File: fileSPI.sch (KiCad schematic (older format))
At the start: 6 parts, among them U18 74HC165, U25 74AHCT595, U6 74AHC273

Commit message: Renaming files, cleaning, CHANGELOG
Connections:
- net BCSPI_CLK renamed BCFG_SPI_CLK
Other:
- moved on the sheet: C41
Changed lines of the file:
@@
 L Device:C C?
 U 1 1 5DD64D25
-P 2100 3500
+P 1950 3500
 AR Path="/5ACA3361/5DD64D25" Ref="C?"  Part="1"
 AR Path="/5DD53CC6/5DD64D25" Ref="C41"  Part="1"
-F 0 "C41" H 2125 3600 50  0000 L CNN
-F 1 "10nF" H 2125 3400 50  0000 L CNN
-F 2 "Capacitor_SMD:C_0805_2012Metric" H 2138 3350 50  0001 C CNN
-F 3 "" H 2100 3500 50  0001 C CNN
-	1    2100 3500
+F 0 "C41" H 1975 3600 50  0000 L CNN
+F 1 "10nF" H 1975 3400 50  0000 L CNN
+F 2 "Capacitor_SMD:C_0805_2012Metric" H 1988 3350 50  0001 C CNN
+F 3 "" H 1950 3500 50  0001 C CNN
+	1    1950 3500
 	-1   0    0    1
 $EndComp
@@
 Wire Wire Line
 	3150 3650 3150 3600
-Wire Wire Line
-	2100 3650 3150 3650
-Wire Wire Line
-	2100 3350 2100 3300
-Wire Wire Line
-	2100 1950 3150 1950
-Wire Wire Line
-	2650 3300 2100 3300
-Connection ~ 2100 3300
 Text Label 3650 2300 0    60   ~ 0
 SPI_CFG_~PL
@@
 SPI_CLK
 Text Label 1500 1650 0    60   ~ 0
-BCSPI_CLK
+BCFG_SPI_CLK
 Text HLabel 1450 1550 0    60   Input ~ 0
 SPI_CLK
 Text HLabel 1450 1650 0    60   Input ~ 0
-BCSPI_CLK
+BCFG_SPI_CLK
 Wire Wire Line
 	1450 1550 1500 1550
@@
 Text Label 5100 3300 2    60   ~ 0
 SPI_CFG_~PL
-Text Label 2650 3200 2    60   ~ 0
-BCSPI_CLK
-Wire Wire Line
-	2100 1950 2100 3300
 Text Label 2650 2700 2    60   ~ 0
 NUMBER_4
@@
 Text Label 5100 2700 2    60   ~ 0
 BUFF_3
+Text Label 2650 3200 2    60   ~ 0
+BCFG_SPI_CLK
+Wire Wire Line
+	1950 3650 3150 3650
+Wire Wire Line
+	1950 3350 1950 3300
+Wire Wire Line
+	1950 1950 3150 1950
+Connection ~ 1950 3300
+Wire Wire Line
+	1950 3300 1950 1950
+Wire Wire Line
+	1950 3300 2650 3300
 Wire Bus Line
 	1550 4750 1550 5550

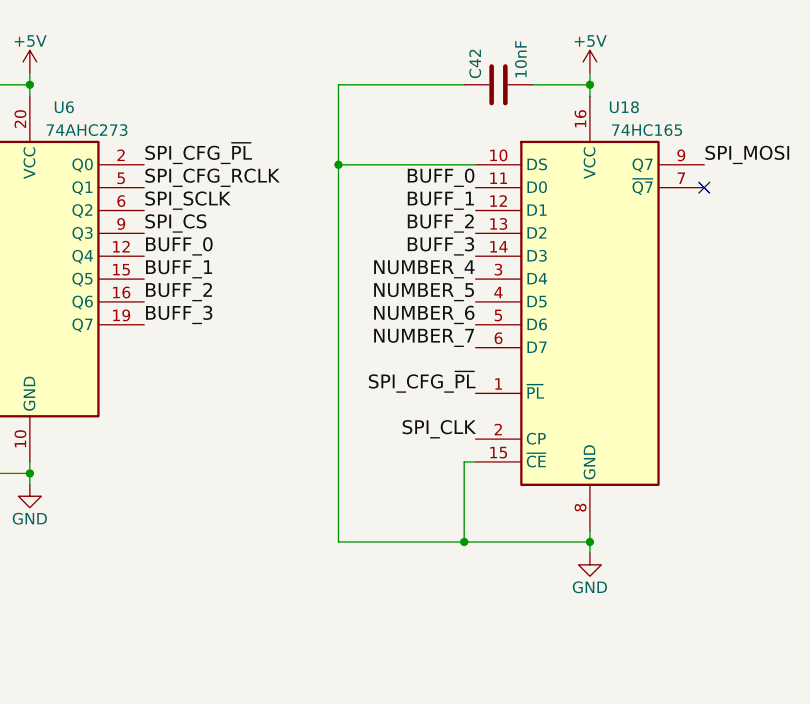
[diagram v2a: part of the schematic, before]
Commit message: Revert SPI 4bits problem work-around (finally this fixed nothing)
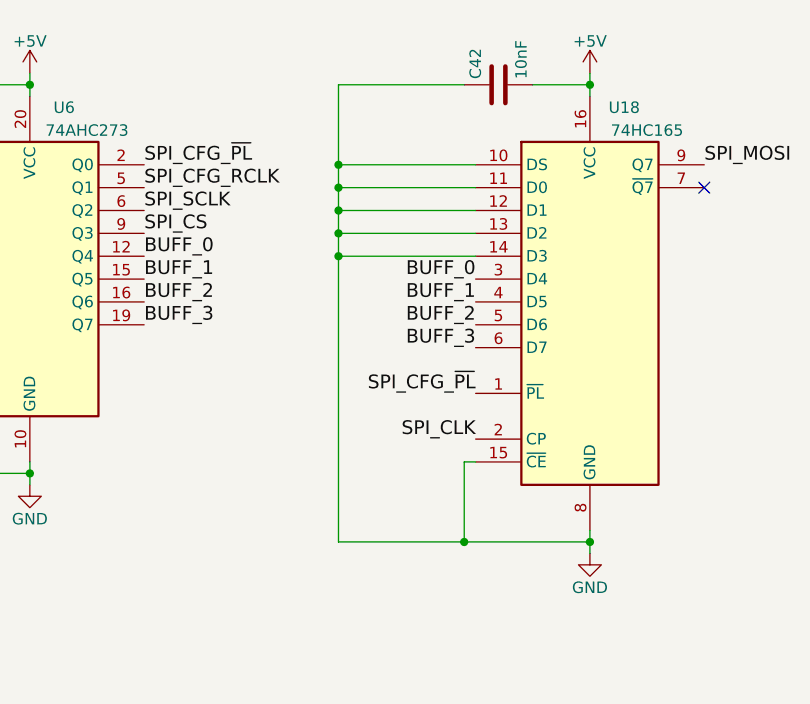
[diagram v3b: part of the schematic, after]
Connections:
- net BUFF_0: now also U18.3 (D4); no longer U18.11 (D0)
- net BUFF_1: now also U18.4 (D5); no longer U18.12 (D1)
- net BUFF_2: now also U18.5 (D6); no longer U18.13 (D2)
- net BUFF_3: now also U18.6 (D7); no longer U18.14 (D3)
- net GND: now also U18.11 (D0), U18.12 (D1), U18.13 (D2), U18.14 (D3)
- net NUMBER_4: no longer U18.3 (D4)
- net NUMBER_5: no longer U18.4 (D5)
- net NUMBER_6: no longer U18.5 (D6)
- net NUMBER_7: no longer U18.6 (D7)
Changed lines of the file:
@@
 Text Label 3650 2300 0    60   ~ 0
 SPI_CFG_~PL
-Text Label 3650 2500 0    60   ~ 0
-SPI_SCLK
 Text Label 5100 3500 2    60   ~ 0
 SPI_CLK
 Text Label 3650 2600 0    60   ~ 0
 SPI_CS
-Text Label 5100 2800 2    60   ~ 0
-NUMBER_4
-Text Label 5100 2900 2    60   ~ 0
-NUMBER_5
-Text Label 5100 3000 2    60   ~ 0
-NUMBER_6
-Text Label 5100 3100 2    60   ~ 0
-NUMBER_7
-Text Label 3650 2400 0    60   ~ 0
-SPI_CFG_RCLK
 Text Label 7500 2800 2    60   ~ 0
 SPI_CFG_RCLK
@@
 	5100 2300 4500 2300
 Wire Wire Line
-	4500 2300 4500 3950
+	4500 2300 4500 2400
 Wire Wire Line
 	4500 3950 5050 3950
@@
 Text Label 3650 3000 0    60   ~ 0
 BUFF_3
-Text Label 5100 2400 2    60   ~ 0
-BUFF_0
-Text Label 5100 2500 2    60   ~ 0
-BUFF_1
-Text Label 5100 2600 2    60   ~ 0
-BUFF_2
-Text Label 5100 2700 2    60   ~ 0
-BUFF_3
 Text Label 2650 3200 2    60   ~ 0
 BCFG_SPI_CLK
@@
 Wire Wire Line
 	1950 3300 2650 3300
+Text Label 3650 2400 0    60   ~ 0
+SPI_CFG_RCLK
+Text Label 3650 2500 0    60   ~ 0
+SPI_SCLK
+Text Label 5100 2800 2    60   ~ 0
+BUFF_0
+Text Label 5100 2900 2    60   ~ 0
+BUFF_1
+Text Label 5100 3000 2    60   ~ 0
+BUFF_2
+Text Label 5100 3100 2    60   ~ 0
+BUFF_3
+Wire Wire Line
+	5100 2400 4500 2400
+Connection ~ 4500 2400
+Wire Wire Line
+	4500 2400 4500 2500
+Wire Wire Line
+	5100 2500 4500 2500
+Connection ~ 4500 2500
+Wire Wire Line
+	4500 2500 4500 2600
+Wire Wire Line
+	5100 2600 4500 2600
+Connection ~ 4500 2600
+Wire Wire Line
+	4500 2600 4500 2700
+Wire Wire Line
+	5100 2700 4500 2700
 Wire Bus Line
 	1550 4750 1550 5550
+Connection ~ 4500 2700
+Wire Wire Line
+	4500 2700 4500 3950
 $EndSCHEMATC

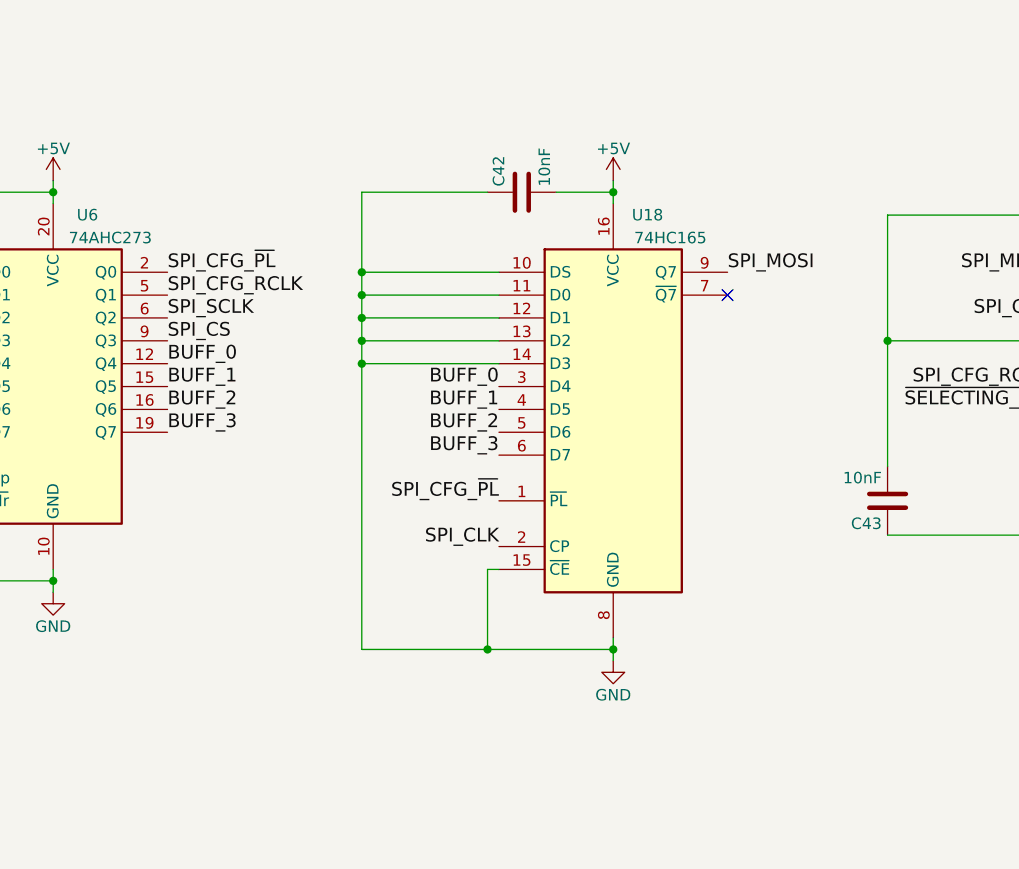
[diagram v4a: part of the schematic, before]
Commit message: V5.1 (#9)
* Apply new symbol for XC2C256-VQ100 #5

* Set new date and 5.1

* Replacing 74HC165 with 74HC166, and add SPI_CFG_DS #4

* Replace some gates with a 74AHC1G02 to fix the pulse problem #3

* Go next only if SRCVALUE, (simple instruction)

* Remove weird ghost bus in register

* Small cleaning in fileRegister

* Go next only if SRCVALUE, (complex instruction) #8
adding 74AHC1G08

* Better decoupling #6

* Component association (#7)

* netlist

* Updated BOM for V5.1

* Routing, cleaning first pass

* bit of pcb cleaning

* SolderMaskClearance to 0

* Schematics to pdf

* PCB files in pdf

* exporting Gerbert files

* new 3d images

* Update README.md

* Modifying CHANGELOG file

* Update README.md
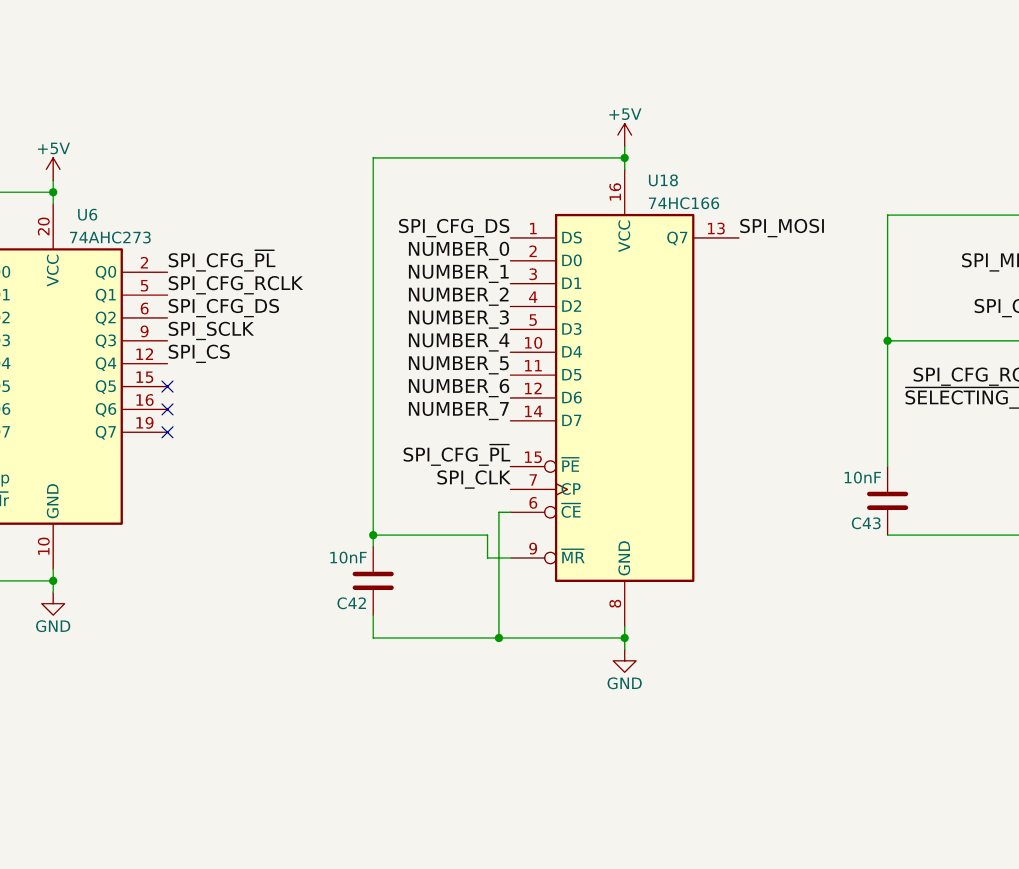
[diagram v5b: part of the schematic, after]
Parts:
- removed U18: 74HC165, Package_SO:SOIC-16_3.9x9.9mm_P1.27mm, symbol 74xx:74LS165
- added U18: 74HC166, Package_SO:SOIC-16_3.9x9.9mm_P1.27mm, symbol Custom:74HC166
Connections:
- net BUFF_0 is gone; now on net SPI_CS: U6.12 (Q4)
- net +5V: now also U18.16 (VCC), U18.9 (~MR)
- net GND: now also U18.6 (~CE), U18.8 (GND)
- net NUMBER_0: now also U18.2 (D0)
- net NUMBER_1: now also U18.3 (D1)
- net NUMBER_2: now also U18.4 (D2)
- net NUMBER_3: now also U18.5 (D3)
- net NUMBER_4: now also U18.10 (D4)
- net NUMBER_5: now also U18.11 (D5)
- net NUMBER_6: now also U18.12 (D6)
- net NUMBER_7: now also U18.14 (D7)
- net SPI_CFG_~PL: now also U18.15 (~PE)
- net SPI_CLK: now also U18.7 (CP)
- net SPI_CS: no longer U6.9 (Q3)
- net SPI_MOSI: now also U18.13 (Q7)
- net SPI_SCLK: now also U6.9 (Q3); no longer U6.6 (Q2)
- net BUFF_1: no longer names the net of U6.15 (Q5)
- net BUFF_2: no longer names the net of U6.16 (Q6)
- net BUFF_3: no longer names the net of U6.19 (Q7)
- new net SPI_CFG_DS: U18.1 (DS), U6.6 (Q2)
- no-connect marks 2 -> 4
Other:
- moved on the sheet: C42
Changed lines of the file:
@@
 Sheet 7 8
 Title "GP8B"
-Date "2020-08-19"
-Rev "V5.0"
+Date "2021-03-04"
+Rev "V5.1"
 Comp "Guillaume Guillet"
-Comment1 "Copyright Guillaume Guillet 2020"
+Comment1 "Copyright Guillaume Guillet 2021"
 Comment2 "Licensed under CERN-OHL-W v2 or later"
 Comment3 ""
 Comment4 ""
 $EndDescr
-Text Label 6100 2300 0    60   ~ 0
-SPI_MOSI
 Text Label 7500 2300 2    60   ~ 0
 SPI_MISO
@@
 F 3 "http://www.ti.com/lit/ds/symlink/sn74hc595.pdf" H 7900 2700 50  0001 C CNN
 	1    7900 2700
-	1    0    0    -1
-$EndComp
-$Comp
-L 74xx:74LS165 U18
-U 1 1 5DD58078
-P 5600 2900
-F 0 "U18" H 5750 3750 50  0000 C CNN
-F 1 "74HC165" H 5850 3650 50  0000 C CNN
-F 2 "Package_SO:SOIC-16_3.9x9.9mm_P1.27mm" H 5600 2900 50  0001 C CNN
-F 3 "http://www.ti.com/lit/gpn/sn74LS165" H 5600 2900 50  0001 C CNN
-	1    5600 2900
 	1    0    0    -1
 $EndComp
@@
 Text Label 3650 2300 0    60   ~ 0
 SPI_CFG_~PL
-Text Label 5100 3500 2    60   ~ 0
-SPI_CLK
-Text Label 3650 2600 0    60   ~ 0
+Text Label 3650 2700 0    60   ~ 0
 SPI_CS
 Text Label 7500 2800 2    60   ~ 0
@@
 L power:+5V #PWR?
 U 1 1 5DD8BC4C
-P 5600 1900
+P 5650 1750
 AR Path="/5ACA3361/5DD8BC4C" Ref="#PWR?"  Part="1"
 AR Path="/5DD53CC6/5DD8BC4C" Ref="#PWR0135"  Part="1"
-F 0 "#PWR0135" H 5600 1750 50  0001 C CNN
-F 1 "+5V" H 5600 2040 50  0000 C CNN
-F 2 "" H 5600 1900 50  0001 C CNN
-F 3 "" H 5600 1900 50  0001 C CNN
-	1    5600 1900
+F 0 "#PWR0135" H 5650 1600 50  0001 C CNN
+F 1 "+5V" H 5650 1890 50  0000 C CNN
+F 2 "" H 5650 1750 50  0001 C CNN
+F 3 "" H 5650 1750 50  0001 C CNN
+	1    5650 1750
 	1    0    0    -1
 $EndComp
@@
 L power:GND #PWR?
 U 1 1 5DD8C055
-P 5600 4000
+P 5650 3950
 AR Path="/5ACA3361/5DD8C055" Ref="#PWR?"  Part="1"
 AR Path="/5DD53CC6/5DD8C055" Ref="#PWR0136"  Part="1"
-F 0 "#PWR0136" H 5600 3750 50  0001 C CNN
-F 1 "GND" H 5600 3850 50  0000 C CNN
-F 2 "" H 5600 4000 50  0001 C CNN
-F 3 "" H 5600 4000 50  0001 C CNN
-	1    5600 4000
+F 0 "#PWR0136" H 5650 3700 50  0001 C CNN
+F 1 "GND" H 5650 3800 50  0000 C CNN
+F 2 "" H 5650 3950 50  0001 C CNN
+F 3 "" H 5650 3950 50  0001 C CNN
+	1    5650 3950
 	1    0    0    -1
 $EndComp
@@
 L Device:C C?
 U 1 1 5DD8C9C7
-P 5200 1950
+P 4550 3650
 AR Path="/5ACA3361/5DD8C9C7" Ref="C?"  Part="1"
 AR Path="/5DD53CC6/5DD8C9C7" Ref="C42"  Part="1"
-F 0 "C42" H 5225 2050 50  0000 L CNN
-F 1 "10nF" H 5225 1850 50  0000 L CNN
-F 2 "Capacitor_SMD:C_0805_2012Metric" H 5238 1800 50  0001 C CNN
-F 3 "" H 5200 1950 50  0001 C CNN
-	1    5200 1950
-	0    -1   -1   0
+F 0 "C42" H 4575 3750 50  0000 L CNN
+F 1 "10nF" H 4575 3550 50  0000 L CNN
+F 2 "Capacitor_SMD:C_0805_2012Metric" H 4588 3500 50  0001 C CNN
+F 3 "" H 4550 3650 50  0001 C CNN
+	1    4550 3650
+	-1   0    0    1
 $EndComp
 $Comp
@@
 $EndComp
 Wire Wire Line
-	5600 3950 5600 3900
-Wire Wire Line
-	5600 3950 5600 4000
-Connection ~ 5600 3950
-Wire Wire Line
-	5100 3600 5050 3600
-Wire Wire Line
-	5050 3600 5050 3950
-Connection ~ 5050 3950
-Wire Wire Line
-	5050 3950 5600 3950
+	5650 3900 5650 3850
+Wire Wire Line
+	5650 3900 5650 3950
+Connection ~ 5650 3900
+Connection ~ 5100 3900
+Wire Wire Line
+	5100 3900 5650 3900
 Wire Wire Line
 	7900 3500 7900 3450
@@
 SPI_CS
 Wire Wire Line
-	5600 1900 5600 1950
-Wire Wire Line
-	5100 2300 4500 2300
-Wire Wire Line
-	4500 2300 4500 2400
-Wire Wire Line
-	4500 3950 5050 3950
-Wire Wire Line
-	4500 2300 4500 1950
-Wire Wire Line
-	4500 1950 5050 1950
-Connection ~ 4500 2300
-Wire Wire Line
-	5350 1950 5600 1950
-Connection ~ 5600 1950
-Wire Wire Line
-	5600 1950 5600 2000
+	5650 1750 5650 1800
+Wire Wire Line
+	4550 3900 5100 3900
+Connection ~ 5650 1800
+Wire Wire Line
+	5650 1800 5650 1850
 Text Label 9450 1450 2    60   ~ 0
 SPI_SCLK
@@
 Text Label 1500 1450 0    60   ~ 0
 SPI_MISO
-NoConn ~ 6100 2400
 NoConn ~ 8300 3200
 Text HLabel 1450 1450 0    60   Input ~ 0
@@
 Text Label 7500 2500 2    60   ~ 0
 SPI_CLK
-Text Label 5100 3300 2    60   ~ 0
-SPI_CFG_~PL
 Text Label 2650 2700 2    60   ~ 0
 NUMBER_4
@@
 Text Label 2650 3000 2    60   ~ 0
 NUMBER_7
-Text Label 3650 2700 0    60   ~ 0
-BUFF_0
-Text Label 3650 2800 0    60   ~ 0
-BUFF_1
-Text Label 3650 2900 0    60   ~ 0
-BUFF_2
-Text Label 3650 3000 0    60   ~ 0
-BUFF_3
 Text Label 2650 3200 2    60   ~ 0
 BCFG_SPI_CLK
@@
 Text Label 3650 2400 0    60   ~ 0
 SPI_CFG_RCLK
+Text Label 3650 2600 0    60   ~ 0
+SPI_SCLK
+$Comp
+L Custom:74HC166 U18
+U 1 1 60417A96
+P 5650 2850
+F 0 "U18" H 5750 3800 50  0000 L CNN
+F 1 "74HC166" H 5750 3700 50  0000 L CNN
+F 2 "Package_SO:SOIC-16_3.9x9.9mm_P1.27mm" H 5650 2850 50  0001 C CNN
+F 3 "https://assets.nexperia.com/documents/data-sheet/74HC_HCT166.pdf" H 5650 2850 50  0001 C CNN
+	1    5650 2850
+	1    0    0    -1
+$EndComp
+Text Label 5150 2250 2    60   ~ 0
+NUMBER_0
+Text Label 5150 2350 2    60   ~ 0
+NUMBER_1
+Text Label 5150 2450 2    60   ~ 0
+NUMBER_2
+Text Label 5150 2550 2    60   ~ 0
+NUMBER_3
+Text Label 5150 2650 2    60   ~ 0
+NUMBER_4
+Text Label 5150 2750 2    60   ~ 0
+NUMBER_5
+Text Label 5150 2850 2    60   ~ 0
+NUMBER_6
+Text Label 5150 2950 2    60   ~ 0
+NUMBER_7
+Text Label 5150 3250 2    60   ~ 0
+SPI_CLK
+Text Label 6150 2150 0    60   ~ 0
+SPI_MOSI
+Wire Wire Line
+	5150 3350 5100 3350
+Wire Wire Line
+	5100 3350 5100 3900
+Wire Wire Line
+	4550 1800 4550 3450
+Wire Wire Line
+	4550 3900 4550 3800
+Wire Wire Line
+	4550 3450 5050 3450
+Connection ~ 4550 3450
+Wire Wire Line
+	4550 3450 4550 3500
+Wire Wire Line
+	5050 3450 5050 3550
+Wire Wire Line
+	5050 3550 5150 3550
+Text Label 5150 3150 2    60   ~ 0
+SPI_CFG_~PL
 Text Label 3650 2500 0    60   ~ 0
-SPI_SCLK
-Text Label 5100 2800 2    60   ~ 0
-BUFF_0
-Text Label 5100 2900 2    60   ~ 0
-BUFF_1
-Text Label 5100 3000 2    60   ~ 0
-BUFF_2
-Text Label 5100 3100 2    60   ~ 0
-BUFF_3
-Wire Wire Line
-	5100 2400 4500 2400
-Connection ~ 4500 2400
-Wire Wire Line
-	4500 2400 4500 2500
-Wire Wire Line
-	5100 2500 4500 2500
-Connection ~ 4500 2500
-Wire Wire Line
-	4500 2500 4500 2600
-Wire Wire Line
-	5100 2600 4500 2600
-Connection ~ 4500 2600
-Wire Wire Line
-	4500 2600 4500 2700
-Wire Wire Line
-	5100 2700 4500 2700
+SPI_CFG_DS
+Text Label 5150 2150 2    60   ~ 0
+SPI_CFG_DS
+Wire Wire Line
+	4550 1800 5650 1800
+NoConn ~ 3650 2800
+NoConn ~ 3650 2900
+NoConn ~ 3650 3000
 Wire Bus Line
 	1550 4750 1550 5550
-Connection ~ 4500 2700
-Wire Wire Line
-	4500 2700 4500 3950
 $EndSCHEMATC
